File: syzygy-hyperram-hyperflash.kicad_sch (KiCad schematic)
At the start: 28 parts, among them IC1 ATTINY44A-MMH, IC2 TLV6710DDCT, IC3 S27KL0641DABHI020, IC4 S71KL256SC0BHI, J1 SYZYGY_STD, J2 Conn_02x03_Odd_Even

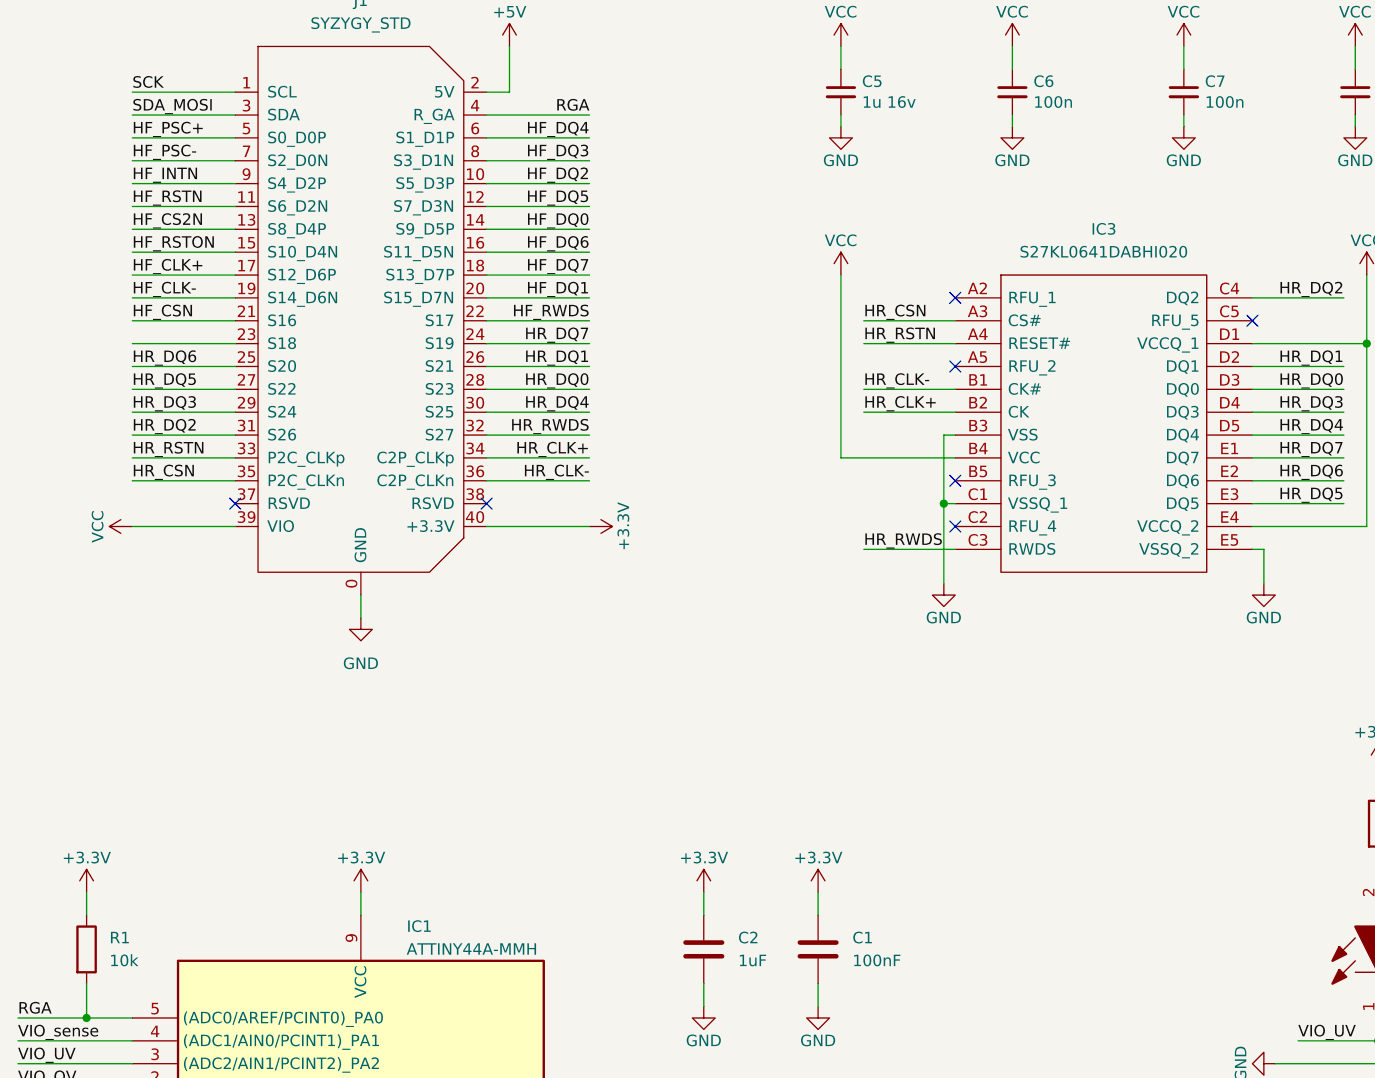
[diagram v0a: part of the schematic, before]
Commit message: Rearranged HyperRAM signals to prioritize data and rwds. Added header with supply voltages.
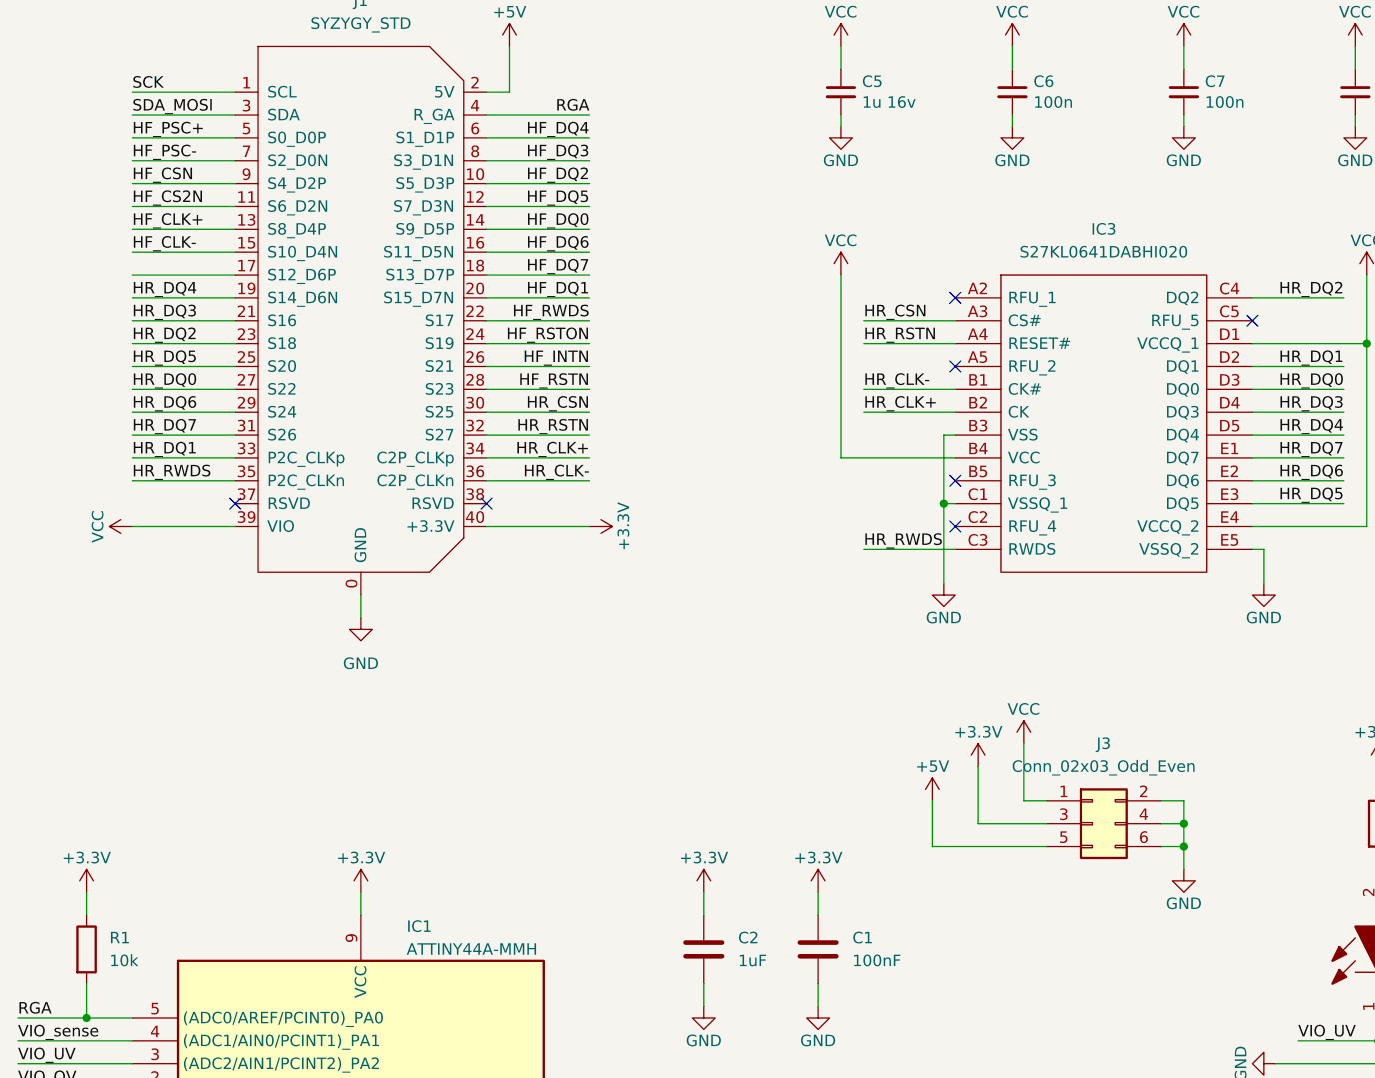
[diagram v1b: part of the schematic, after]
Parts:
- added J3: Conn_02x03_Odd_Even, Connector_PinHeader_2.54mm:PinHeader_2x03_P2.54mm_Vertical, symbol Connector_Generic:Conn_02x03_Odd_Even
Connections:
- net +3.3V: now also J3.3 (Pin_3)
- net +5V: now also J3.5 (Pin_5)
- net GND: now also J3.2 (Pin_2), J3.4 (Pin_4), J3.6 (Pin_6)
- net HF_CLK+: now also J1.13 (S8_D4P); no longer J1.17 (S12_D6P)
- net HF_CLK-: now also J1.15 (S10_D4N); no longer J1.19 (S14_D6N)
- net HF_CS2N: now also J1.11 (S6_D2N); no longer J1.13 (S8_D4P)
- net HF_CSN: now also J1.9 (S4_D2P); no longer J1.21 (S16)
- net HF_INTN: now also J1.26 (S21); no longer J1.9 (S4_D2P)
- net HF_RSTN: now also J1.28 (S23); no longer J1.11 (S6_D2N)
- net HF_RSTON: now also J1.24 (S19); no longer J1.15 (S10_D4N)
- net HR_CSN: now also J1.30 (S25); no longer J1.35 (P2C_CLKn)
- net HR_DQ0: now also J1.27 (S22); no longer J1.28 (S23)
- net HR_DQ1: now also J1.33 (P2C_CLKp); no longer J1.26 (S21)
- net HR_DQ2: now also J1.23 (S18); no longer J1.31 (S26)
- net HR_DQ3: now also J1.21 (S16); no longer J1.29 (S24)
- net HR_DQ4: now also J1.19 (S14_D6N); no longer J1.30 (S25)
- net HR_DQ5: now also J1.25 (S20); no longer J1.27 (S22)
- net HR_DQ6: now also J1.29 (S24); no longer J1.25 (S20)
- net HR_DQ7: now also J1.31 (S26); no longer J1.24 (S19)
- net HR_RSTN: now also J1.32 (S27); no longer J1.33 (P2C_CLKp)
- net HR_RWDS: now also J1.35 (P2C_CLKn); no longer J1.32 (S27)
- net VCC: now also J3.1 (Pin_1)

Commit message: Rearranging HyperRAM (IC3) signals to simplify routing
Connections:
- net HF_DQ1: now also J1.10 (S5_D3P); no longer J1.20 (S15_D7N)
- net HF_DQ2: now also J1.18 (S13_D7P); no longer J1.10 (S5_D3P)
- net HF_DQ3: now also J1.20 (S15_D7N); no longer J1.8 (S3_D1N)
- net HF_DQ4: now also J1.22 (S17); no longer J1.6 (S1_D1P)
- net HF_DQ5: now also J1.16 (S11_D5N); no longer J1.12 (S7_D3N)
- net HF_DQ6: now also J1.12 (S7_D3N); no longer J1.16 (S11_D5N)
- net HF_DQ7: now also J1.8 (S3_D1N); no longer J1.18 (S13_D7P)
- net HF_RWDS: now also J1.6 (S1_D1P); no longer J1.22 (S17)
- net HR_CSN: now also J1.17 (S12_D6P); no longer J1.30 (S25)
- net HR_DQ1: now also J1.23 (S18); no longer J1.33 (P2C_CLKp)
- net HR_DQ2: now also J1.31 (S26); no longer J1.23 (S18)
- net HR_DQ3: now also J1.33 (P2C_CLKp); no longer J1.21 (S16)
- net HR_DQ4: now also J1.35 (P2C_CLKn); no longer J1.19 (S14_D6N)
- net HR_DQ5: now also J1.29 (S24); no longer J1.25 (S20)
- net HR_DQ6: now also J1.25 (S20); no longer J1.29 (S24)
- net HR_DQ7: now also J1.21 (S16); no longer J1.31 (S26)
- net HR_RWDS: now also J1.19 (S14_D6N); no longer J1.35 (P2C_CLKn)
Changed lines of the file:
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@@
 	)
 	(label "HF_DQ4"
-		(at 101.6 38.1 180)
+		(at 101.6 58.42 180)
 		(fields_autoplaced yes)
 		(effects
@@
 	)
 	(label "HF_DQ3"
-		(at 101.6 40.64 180)
+		(at 101.6 55.88 180)
 		(fields_autoplaced yes)
 		(effects
@@
 	)
 	(label "HF_RWDS"
-		(at 101.6 58.42 180)
+		(at 101.6 38.1 180)
 		(fields_autoplaced yes)
 		(effects
@@
 	)
 	(label "HR_DQ2"
-		(at 50.8 60.96 0)
+		(at 50.8 71.12 0)
 		(fields_autoplaced yes)
 		(effects
@@
 	)
 	(label "HF_DQ1"
-		(at 101.6 55.88 180)
+		(at 101.6 43.18 180)
 		(fields_autoplaced yes)
 		(effects
@@
 	)
 	(label "HF_DQ7"
-		(at 101.6 53.34 180)
+		(at 101.6 40.64 180)
 		(fields_autoplaced yes)
 		(effects
@@
 	)
 	(label "HR_CSN"
-		(at 101.6 68.58 180)
-		(fields_autoplaced yes)
-		(effects
-			(font
-				(size 1.27 1.27)
-			)
-			(justify right bottom)
+		(at 50.8 53.34 0)
+		(fields_autoplaced yes)
+		(effects
+			(font
+				(size 1.27 1.27)
+			)
+			(justify left bottom)
 		)
 	)
@@
 	)
 	(label "HF_DQ5"
-		(at 101.6 45.72 180)
+		(at 101.6 50.8 180)
 		(fields_autoplaced yes)
 		(effects
@@
 	)
 	(label "HF_DQ2"
-		(at 101.6 43.18 180)
+		(at 101.6 53.34 180)
 		(fields_autoplaced yes)
 		(effects
@@
 	)
 	(label "HF_DQ6"
-		(at 101.6 50.8 180)
+		(at 101.6 45.72 180)
 		(fields_autoplaced yes)
 		(effects
@@
 	)
 	(label "HR_DQ5"
-		(at 50.8 63.5 0)
+		(at 50.8 68.58 0)
 		(fields_autoplaced yes)
 		(effects
@@
 	)
 	(label "HR_DQ3"
-		(at 50.8 58.42 0)
+		(at 50.8 73.66 0)
 		(fields_autoplaced yes)
 		(effects
@@
 	)
 	(label "HR_DQ1"
-		(at 50.8 73.66 0)
+		(at 50.8 60.96 0)
 		(fields_autoplaced yes)
 		(effects
@@
 	)
 	(label "HR_DQ4"
-		(at 50.8 55.88 0)
+		(at 50.8 76.2 0)
 		(fields_autoplaced yes)
 		(effects
@@
 	)
 	(label "HR_DQ6"
-		(at 50.8 68.58 0)
+		(at 50.8 63.5 0)
 		(fields_autoplaced yes)
 		(effects
@@
 	)
 	(label "HR_DQ7"
-		(at 50.8 71.12 0)
+		(at 50.8 58.42 0)
 		(fields_autoplaced yes)
 		(effects
@@
 	)
 	(label "HR_RWDS"
-		(at 50.8 76.2 0)
-		(fields_autoplaced yes)
-		(effects
+		(at 50.8 55.88 0)
+		(fields_autoplaced yes)
+		(effects

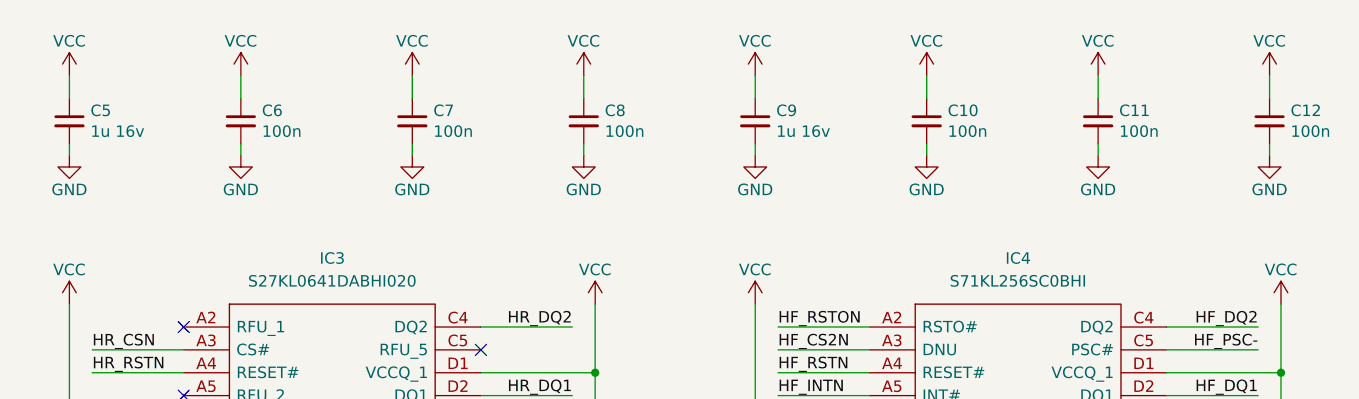
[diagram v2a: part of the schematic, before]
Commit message: Added more filtering capacitors for HyperRAM and HyperFLash supply
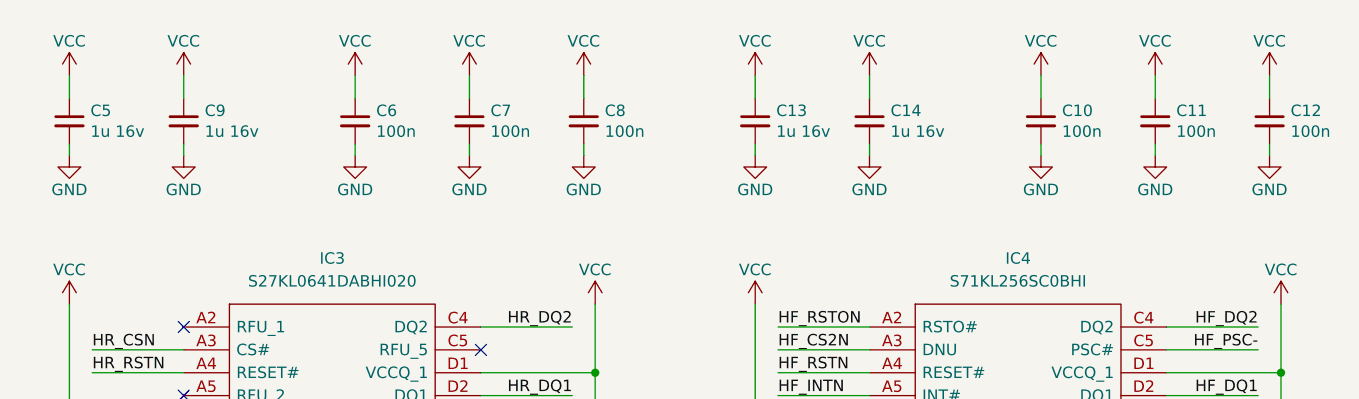
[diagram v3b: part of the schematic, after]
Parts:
- added C13, C14: 1u 16v, Capacitor_SMD:C_0805_2012Metric_Pad1.18x1.45mm_HandSolder, symbol Device:C_Small
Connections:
- net GND: now also C13.2, C14.2
- net VCC: now also C13.1, C14.1
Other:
- moved on the sheet: C10, C11, C6, C7, C9

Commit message: Optimizing signal assignements to simplify routing HyperFlash
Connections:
- net HF_DQ0: now also J1.20 (S15_D7N); no longer J1.14 (S9_D5P)
- net HF_DQ1: now also J1.16 (S11_D5N); no longer J1.10 (S5_D3P)
- net HF_DQ2: now also J1.26 (S21); no longer J1.18 (S13_D7P)
- net HF_DQ3: now also J1.24 (S19); no longer J1.20 (S15_D7N)
- net HF_DQ4: now also J1.28 (S23); no longer J1.22 (S17)
- net HF_DQ5: now also J1.22 (S17); no longer J1.16 (S11_D5N)
- net HF_DQ6: now also J1.18 (S13_D7P); no longer J1.12 (S7_D3N)
- net HF_DQ7: now also J1.14 (S9_D5P); no longer J1.8 (S3_D1N)
- net HF_INTN: now also J1.8 (S3_D1N); no longer J1.26 (S21)
- net HF_RSTN: now also J1.10 (S5_D3P); no longer J1.28 (S23)
- net HF_RSTON: now also J1.6 (S1_D1P); no longer J1.24 (S19)
- net HF_RWDS: now also J1.12 (S7_D3N); no longer J1.6 (S1_D1P)
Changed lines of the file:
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@@
 	)
 	(label "HF_DQ4"
-		(at 101.6 58.42 180)
+		(at 101.6 66.04 180)
 		(fields_autoplaced yes)
 		(effects
@@
 	)
 	(label "HF_DQ3"
-		(at 101.6 55.88 180)
+		(at 101.6 60.96 180)
 		(fields_autoplaced yes)
 		(effects
@@
 	)
 	(label "HF_RSTON"
-		(at 101.6 60.96 180)
+		(at 101.6 38.1 180)
 		(fields_autoplaced yes)
 		(effects
@@
 	)
 	(label "HF_RWDS"
-		(at 101.6 38.1 180)
+		(at 101.6 45.72 180)
 		(fields_autoplaced yes)
 		(effects
@@
 	)
 	(label "HF_RSTN"
-		(at 101.6 66.04 180)
+		(at 101.6 43.18 180)
 		(fields_autoplaced yes)
 		(effects
@@
 	)
 	(label "HF_DQ1"
-		(at 101.6 43.18 180)
+		(at 101.6 50.8 180)
 		(fields_autoplaced yes)
 		(effects
@@
 	)
 	(label "HF_DQ7"
-		(at 101.6 40.64 180)
+		(at 101.6 48.26 180)
 		(fields_autoplaced yes)
 		(effects
@@
 	)
 	(label "HF_DQ5"
-		(at 101.6 50.8 180)
+		(at 101.6 58.42 180)
 		(fields_autoplaced yes)
 		(effects
@@
 	)
 	(label "HF_DQ2"
-		(at 101.6 53.34 180)
+		(at 101.6 63.5 180)
 		(fields_autoplaced yes)
 		(effects
@@
 	)
 	(label "HF_DQ6"
-		(at 101.6 45.72 180)
+		(at 101.6 53.34 180)
 		(fields_autoplaced yes)
 		(effects
@@
 	)
 	(label "HF_INTN"
-		(at 101.6 63.5 180)
+		(at 101.6 40.64 180)
 		(fields_autoplaced yes)
 		(effects
@@
 	)
 	(label "HF_DQ0"
-		(at 101.6 48.26 180)
-		(fields_autoplaced yes)
-		(effects
+		(at 101.6 55.88 180)
+		(fields_autoplaced yes)
+		(effects

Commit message: Rearranged few signals to finish routing HyperFlash
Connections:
- net +3.3V: now also LED1.2, LED2.2; no longer R2.1, R3.1
- net HF_CS2N: now also J1.9 (S4_D2P); no longer J1.11 (S6_D2N)
- net HF_CSN: now also J1.11 (S6_D2N); no longer J1.9 (S4_D2P)
- net HF_RSTN: now also J1.6 (S1_D1P); no longer J1.10 (S5_D3P)
- net HF_RSTON: now also J1.10 (S5_D3P); no longer J1.6 (S1_D1P)
- net VIO_OV: now also R3.2; no longer LED2.1
- net VIO_UV: now also R2.2; no longer LED1.1
- new net: LED2.1, R3.1
- new net: LED1.1, R2.1
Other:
- moved on the sheet: LED1, LED2, R2, R3
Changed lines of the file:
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@@
 	(wire
 		(pts
-			(xy 189.23 118.11) (xy 189.23 120.65)
+			(xy 189.23 125.73) (xy 189.23 128.27)
 		)
 		(stroke
@@
 	(wire
 		(pts
-			(xy 217.17 118.11) (xy 217.17 120.65)
+			(xy 217.17 125.73) (xy 217.17 128.27)
 		)
 		(stroke
@@
 	)
 	(label "HF_CSN"
-		(at 50.8 43.18 0)
+		(at 50.8 45.72 0)
 		(fields_autoplaced yes)
 		(effects
@@
 	)
 	(label "HF_RSTON"
-		(at 101.6 38.1 180)
+		(at 101.6 43.18 180)
 		(fields_autoplaced yes)
 		(effects
@@
 	)
 	(label "HF_RSTN"
-		(at 101.6 43.18 180)
+		(at 101.6 38.1 180)
 		(fields_autoplaced yes)
 		(effects
@@
 	)
 	(label "HF_CS2N"
-		(at 50.8 45.72 0)
+		(at 50.8 43.18 0)
 		(fields_autoplaced yes)
 		(effects
@@
 	(symbol
 		(lib_id "syzygy-hyperram-hyperflash:150080BS75000")
-		(at 217.17 135.89 90)
+		(at 217.17 125.73 90)
 		(unit 1)
 		(exclude_from_sim no)
@@
 		(dnp no)
 		(property "Reference" "LED2"
-			(at 224.79 128.27 0)
+			(at 224.79 118.11 0)
 			(effects
 				(font
@@
 		)
 		(property "Value" "150080VS75000"
-			(at 222.25 124.46 0)
+			(at 222.25 114.3 0)
 			(effects
 				(font
@@
 		)
 		(property "Footprint" "LEDC2012X80N"
-			(at 213.36 123.19 0)
+			(at 213.36 113.03 0)
 			(effects
 				(font
@@
 		)
 		(property "Datasheet" "https://katalog.we-online.com/led/datasheet/150080BS75000.pdf"
-			(at 215.9 123.19 0)
+			(at 215.9 113.03 0)
 			(effects
 				(font
@@
 		)
 		(property "Description" "LED,Wurth Elektronik,150080BS75000 Wurth Elektronik 150080BS75000, WL-SMCW Series Blue LED, 470 nm 2012 (0805) Clear, Rectangle Lens SMD package"
-			(at 218.44 123.19 0)
+			(at 218.44 113.03 0)
 			(effects
 				(font
@@
 		)
 		(property "Height" "0.8"
-			(at 220.98 123.19 0)
+			(at 220.98 113.03 0)
 			(effects
 				(font
@@
 		)
 		(property "Mouser Part Number" "710-150080BS75000"
-			(at 223.52 123.19 0)
+			(at 223.52 113.03 0)
 			(effects
 				(font
@@
 		)
 		(property "Mouser Price/Stock" "https://www.mouser.co.uk/ProductDetail/Wurth-Elektronik/150080BS75000?qs=2kOmHSv6VfT2tBo3UPVqAQ%3D%3D"
-			(at 226.06 123.19 0)
+			(at 226.06 113.03 0)
 			(effects
 				(font
@@
 		)
 		(property "Manufacturer_Name" "Wurth Elektronik"
-			(at 228.6 123.19 0)
+			(at 228.6 113.03 0)
 			(effects
 				(font
@@
 		)
 		(property "Manufacturer_Part_Number" "150080BS75000"
-			(at 231.14 123.19 0)
+			(at 231.14 113.03 0)
 			(effects
 				(font
@@
 	(symbol
 		(lib_id "Device:R")
-		(at 189.23 114.3 0)
+		(at 189.23 132.08 0)
 		(unit 1)
 		(exclude_from_sim no)
@@
 		(fields_autoplaced yes)
 		(property "Reference" "R2"
-			(at 191.77 113.0299 0)
+			(at 191.77 130.8099 0)
 			(effects
 				(font
@@
 		)
 		(property "Value" "220"
-			(at 191.77 115.5699 0)
+			(at 191.77 133.3499 0)
 			(effects
 				(font
@@
 		)
 		(property "Footprint" "Resistor_SMD:R_0603_1608Metric_Pad0.98x0.95mm_HandSolder"
-			(at 187.452 114.3 90)
+			(at 187.452 132.08 90)
 			(effects
 				(font
@@
 		)
 		(property "Datasheet" "~"
-			(at 189.23 114.3 0)
+			(at 189.23 132.08 0)
 			(effects
 				(font
@@
 		)
 		(property "Description" "Resistor"
-			(at 189.23 114.3 0)
+			(at 189.23 132.08 0)
 			(effects
 				(font
@@
 	(symbol
 		(lib_id "syzygy-hyperram-hyperflash:150080VS75000")
-		(at 189.23 135.89 90)
+		(at 189.23 125.73 90)
 		(unit 1)
 		(exclude_from_sim no)
@@
 		(dnp no)
 		(property "Reference" "LED1"
-			(at 196.85 128.27 0)
+			(at 196.85 118.11 0)
 			(effects
 				(font
@@
 		)
 		(property "Value" "150080VS75000"
-			(at 194.31 124.46 0)
+			(at 194.31 114.3 0)
 			(effects
 				(font
@@
 		)
 		(property "Footprint" "LEDC2012X80N"
-			(at 185.42 123.19 0)
+			(at 185.42 113.03 0)
 			(effects
 				(font
@@
 		)
 		(property "Datasheet" "http://katalog.we-online.com/led/datasheet/150080VS75000.pdf"
-			(at 187.96 123.19 0)
+			(at 187.96 113.03 0)
 			(effects
 				(font
@@
 		)
 		(property "Description" "Wurth Elektronik WL-SMCW 570 nm Green LED, 2012 (0805) Clear SMD package"
-			(at 190.5 123.19 0)
+			(at 190.5 113.03 0)
 			(effects
 				(font
@@
 		)
 		(property "Height" "0.8"
-			(at 193.04 123.19 0)
+			(at 193.04 113.03 0)
 			(effects
 				(font
@@
 		)
 		(property "Mouser Part Number" "710-150080VS75000"
-			(at 195.58 123.19 0)
+			(at 195.58 113.03 0)
 			(effects
 				(font
@@
 		)
 		(property "Mouser Price/Stock" "https://www.mouser.co.uk/ProductDetail/Wurth-Elektronik/150080VS75000?qs=LlUlMxKIyB0tGHJmO6%252B0ug%3D%3D"
-			(at 198.12 123.19 0)
+			(at 198.12 113.03 0)
 			(effects
 				(font
@@
 		)
 		(property "Manufacturer_Name" "Wurth Elektronik"
-			(at 200.66 123.19 0)
+			(at 200.66 113.03 0)
 			(effects
 				(font
@@
 		)
 		(property "Manufacturer_Part_Number" "150080VS75000"
-			(at 203.2 123.19 0)
+			(at 203.2 113.03 0)
 			(effects
 				(font
@@
 	(symbol
 		(lib_id "Device:R")
-		(at 217.17 114.3 0)
+		(at 217.17 132.08 0)
 		(unit 1)
 		(exclude_from_sim no)
@@
 		(fields_autoplaced yes)
 		(property "Reference" "R3"
-			(at 219.71 113.0299 0)
+			(at 219.71 130.8099 0)
 			(effects
 				(font
@@
 		)
 		(property "Value" "220"
-			(at 219.71 115.5699 0)
+			(at 219.71 133.3499 0)
 			(effects
 				(font
@@
 		)
 		(property "Footprint" "Resistor_SMD:R_0603_1608Metric_Pad0.98x0.95mm_HandSolder"
-			(at 215.392 114.3 90)
+			(at 215.392 132.08 90)
 			(effects
 				(font
@@
 		)
 		(property "Datasheet" "~"
-			(at 217.17 114.3 0)
+			(at 217.17 132.08 0)
 			(effects
 				(font
@@
 		)
 		(property "Description" "Resistor"
-			(at 217.17 114.3 0)
+			(at 217.17 132.08 0)
 			(effects
 				(font
